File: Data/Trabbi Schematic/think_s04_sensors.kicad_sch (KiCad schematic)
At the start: 4 parts, among them SW1 Gear Selector (D7), U1 Motor Position Sensor (E05), U2 DC/DC High Effect Ref

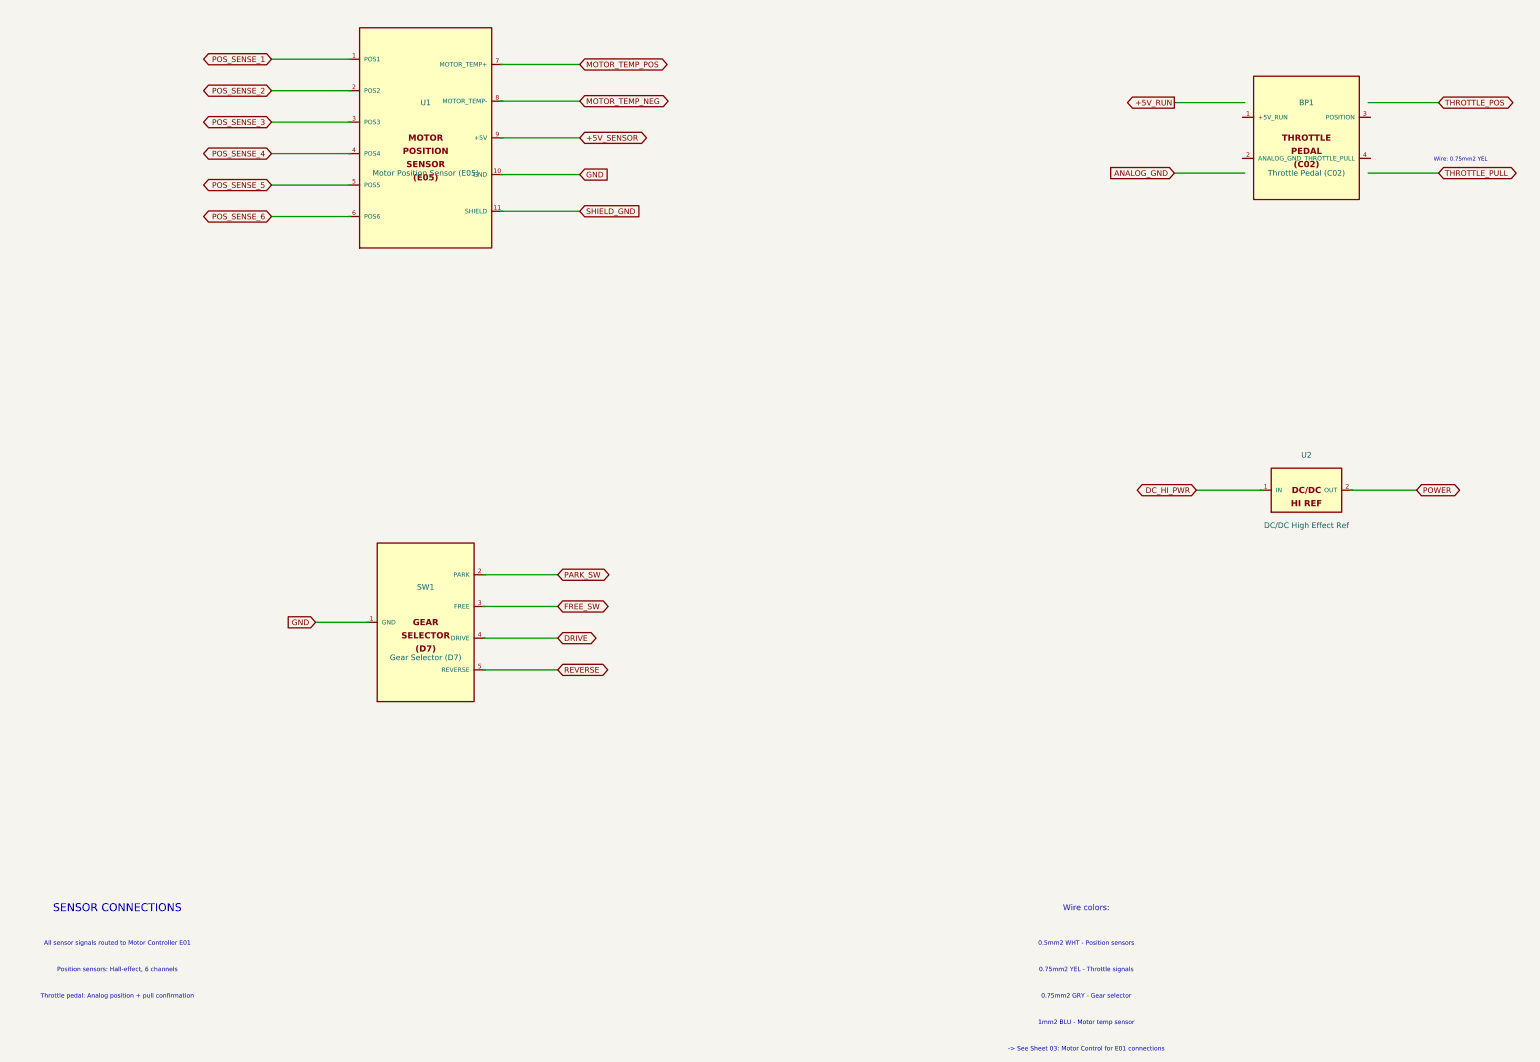
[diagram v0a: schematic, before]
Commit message: Fix wire-to-pin connections: use exact calculated pin positions
Refactored gen_think_complete.py to compute exact pin schematic
coordinates instead of using approximate manual offsets. Added p()
method to Sheet class that transforms symbol-local pin positions to
schematic coordinates. All 232 wire calls across 13 sub-sheet
generators now use p() for pin endpoints, fixing misaligned
connections (previously off by 0.54-10+ units).

Co-Authored-By: Claude Opus 4.6 <noreply@anthropic.com>
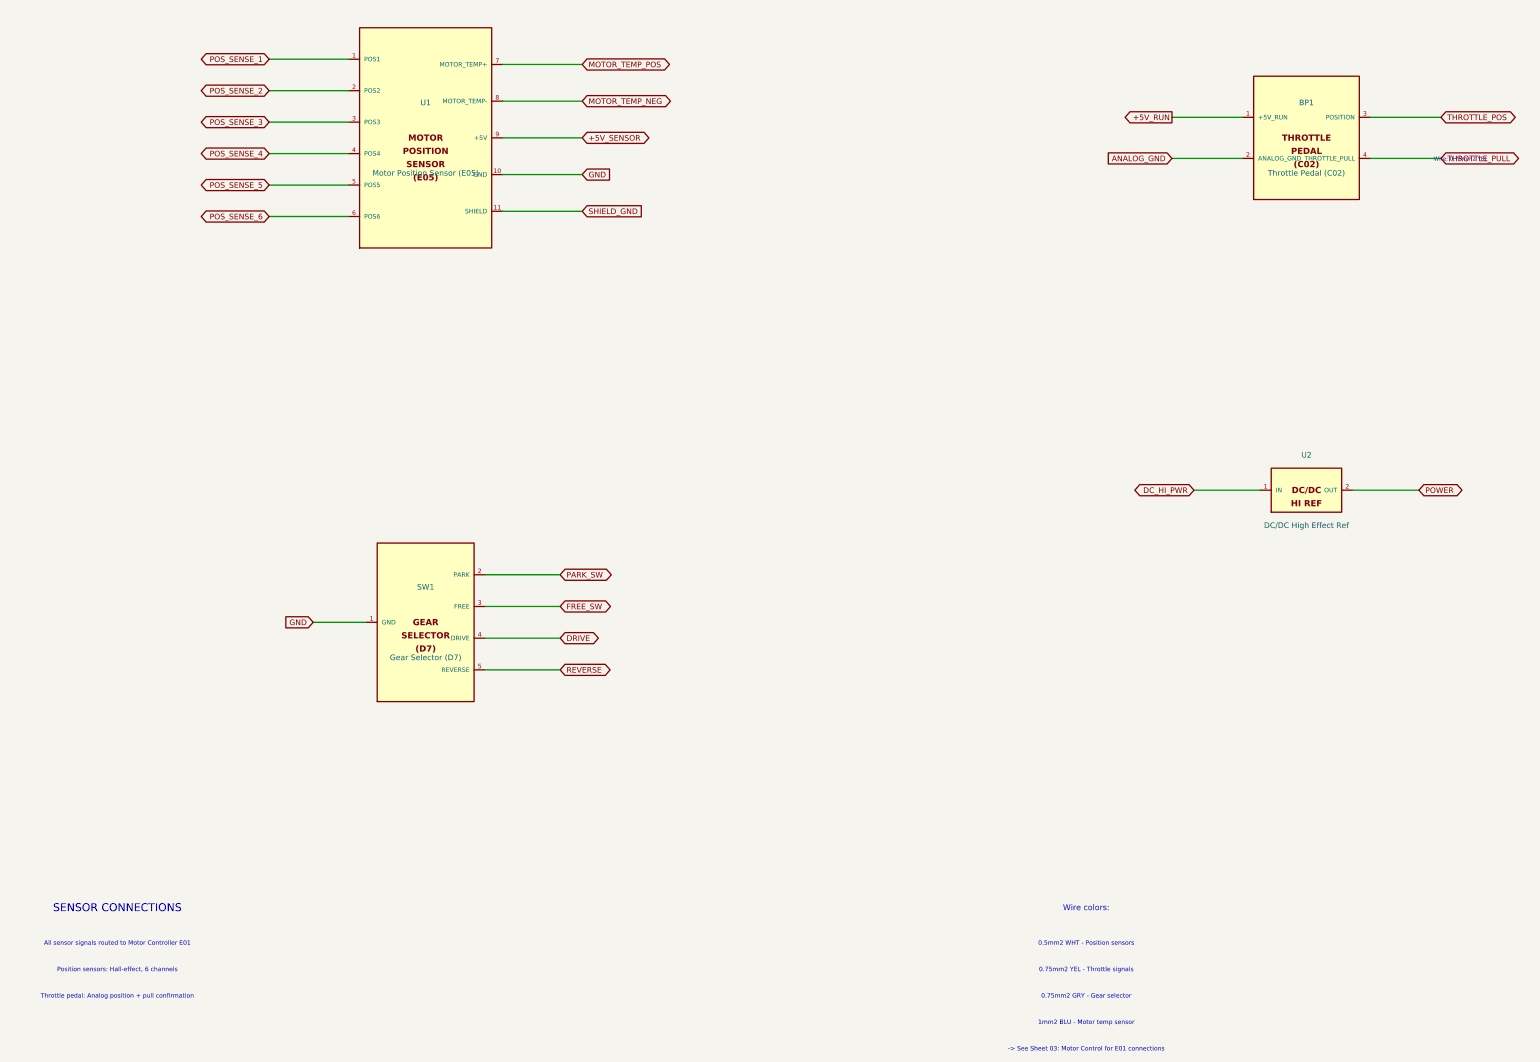
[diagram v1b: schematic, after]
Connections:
- net +5V_RUN: now also BP1.1 (+5V_RUN)
- net +5V_SENSOR: now also U1.9 (+5V)
- net ANALOG_GND: now also BP1.2 (ANALOG_GND)
- net DC_HI_PWR: now also U2.1 (IN)
- net DRIVE: now also SW1.4 (DRIVE)
- net FREE_SW: now also SW1.3 (FREE)
- net GND: now also SW1.1 (GND), U1.10 (GND)
- net MOTOR_TEMP_NEG: now also U1.8 (MOTOR_TEMP-)
- net MOTOR_TEMP_POS: now also U1.7 (MOTOR_TEMP+)
- net PARK_SW: now also SW1.2 (PARK)
- net POS_SENSE_1: now also U1.1 (POS1)
- net POS_SENSE_2: now also U1.2 (POS2)
- net POS_SENSE_3: now also U1.3 (POS3)
- net POS_SENSE_4: now also U1.4 (POS4)
- net POS_SENSE_5: now also U1.5 (POS5)
- net POS_SENSE_6: now also U1.6 (POS6)
- net POWER: now also U2.2 (OUT)
- net REVERSE: now also SW1.5 (REVERSE)
- net SHIELD_GND: now also U1.11 (SHIELD)
- net THROTTLE_POS: now also BP1.3 (POSITION)
- net THROTTLE_PULL: now also BP1.4 (THROTTLE_PULL)

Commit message: Enforce orthogonal routing and 1.27mm grid alignment
- Add _g() grid snap function to Sheet class (rounds all coordinates to nearest 1.27mm)
- Add wire_l() method for L-shaped orthogonal routing (horizontal+vertical segments)
- Apply grid snapping in p(), place(), wire(), label(), glabel(), junction(), no_connect(), defsym()
- Replace all 19 diagonal wire calls with wire_l() across S02, S06, S07, S08, S10, S12, S13
- All wire segments now strictly horizontal or vertical, no diagonals
- All coordinates verified on 1.27mm (50mil) KiCad standard grid

Co-Authored-By: Claude Opus 4.6 <noreply@anthropic.com>
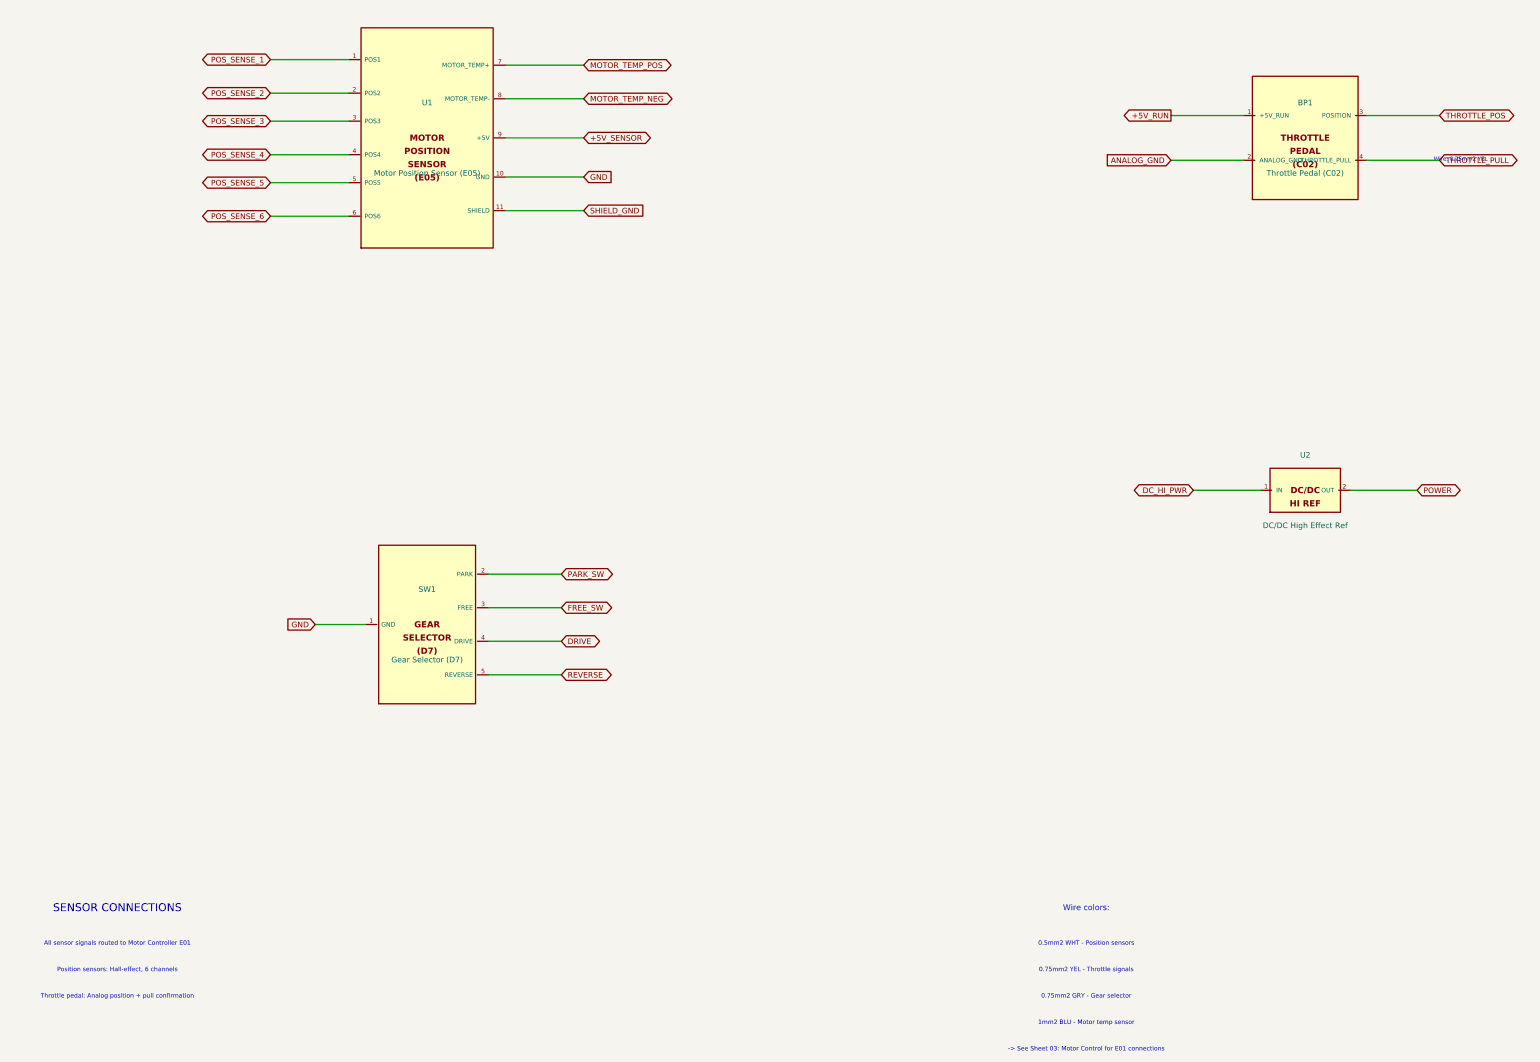
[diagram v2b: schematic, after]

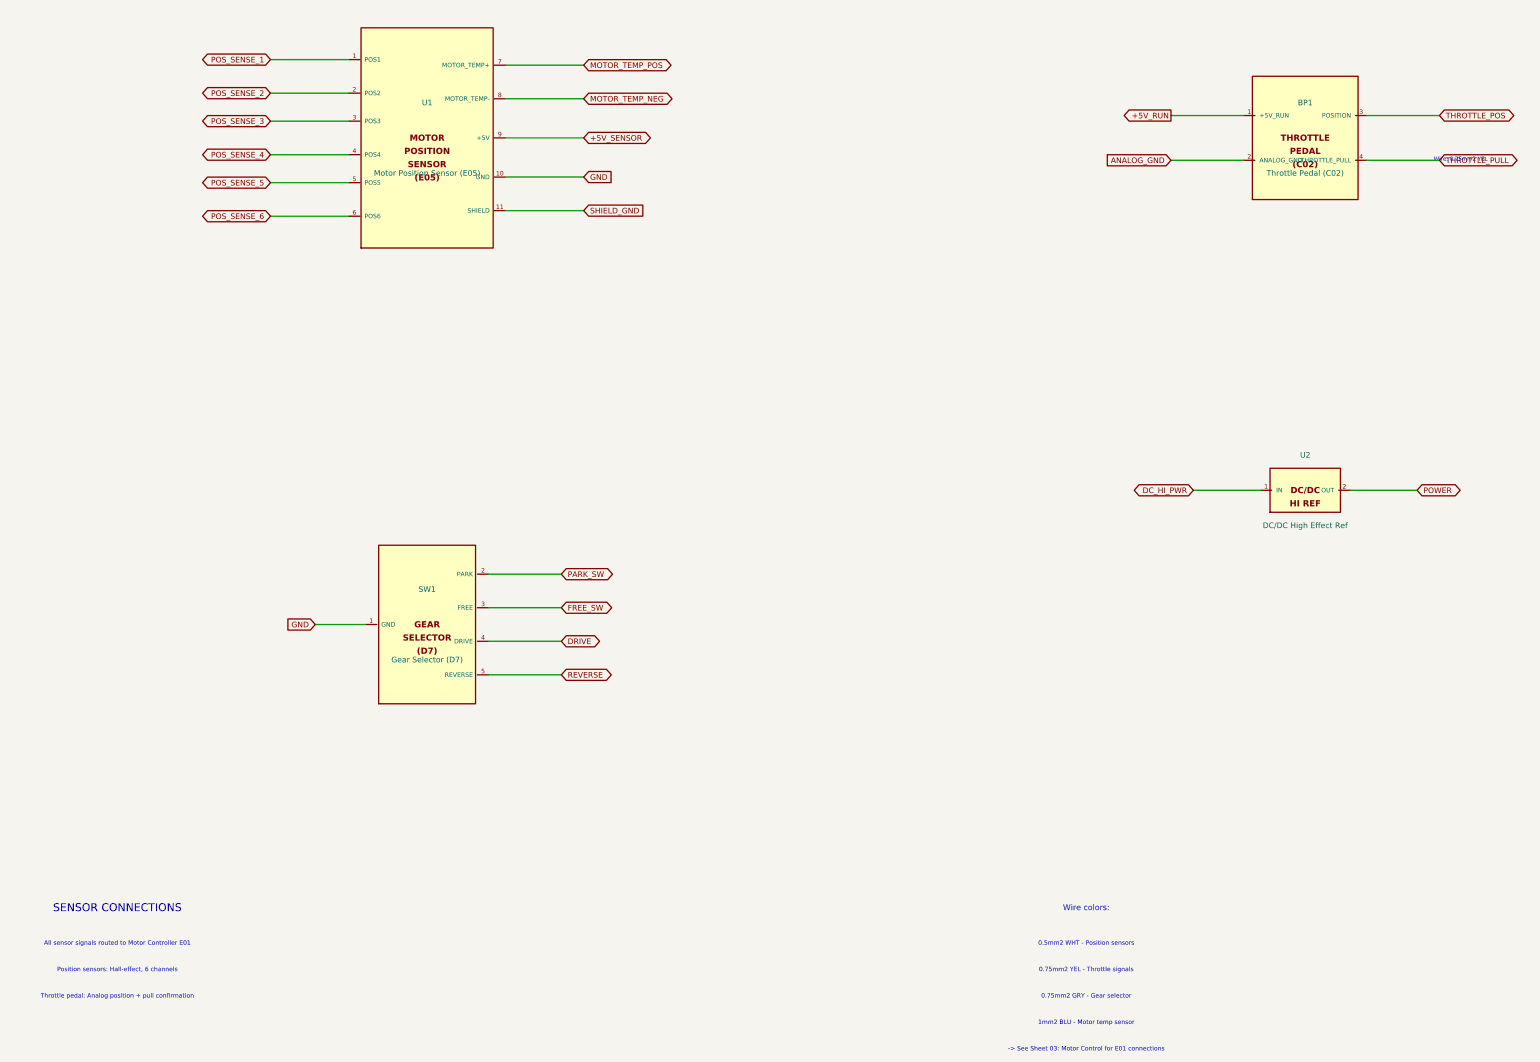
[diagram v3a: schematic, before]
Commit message: Fix label/text positioning: Ref/Value outside body, hide pin numbers
- Reference placed above body edge, Value below (dynamic based on
  symbol height) — no longer overlapping body text
- Pin numbers hidden (clutter, not useful in schematic view)
- Pin name font reduced from 1.016mm to 0.762mm (less overlap)
- Pin length increased from 2.54mm to 3.81mm (more room for pin names
  between body edge and endpoint)
- Store symbol dimensions in _sym_dims for dynamic property placement

Co-Authored-By: Claude Opus 4.6 <noreply@anthropic.com>
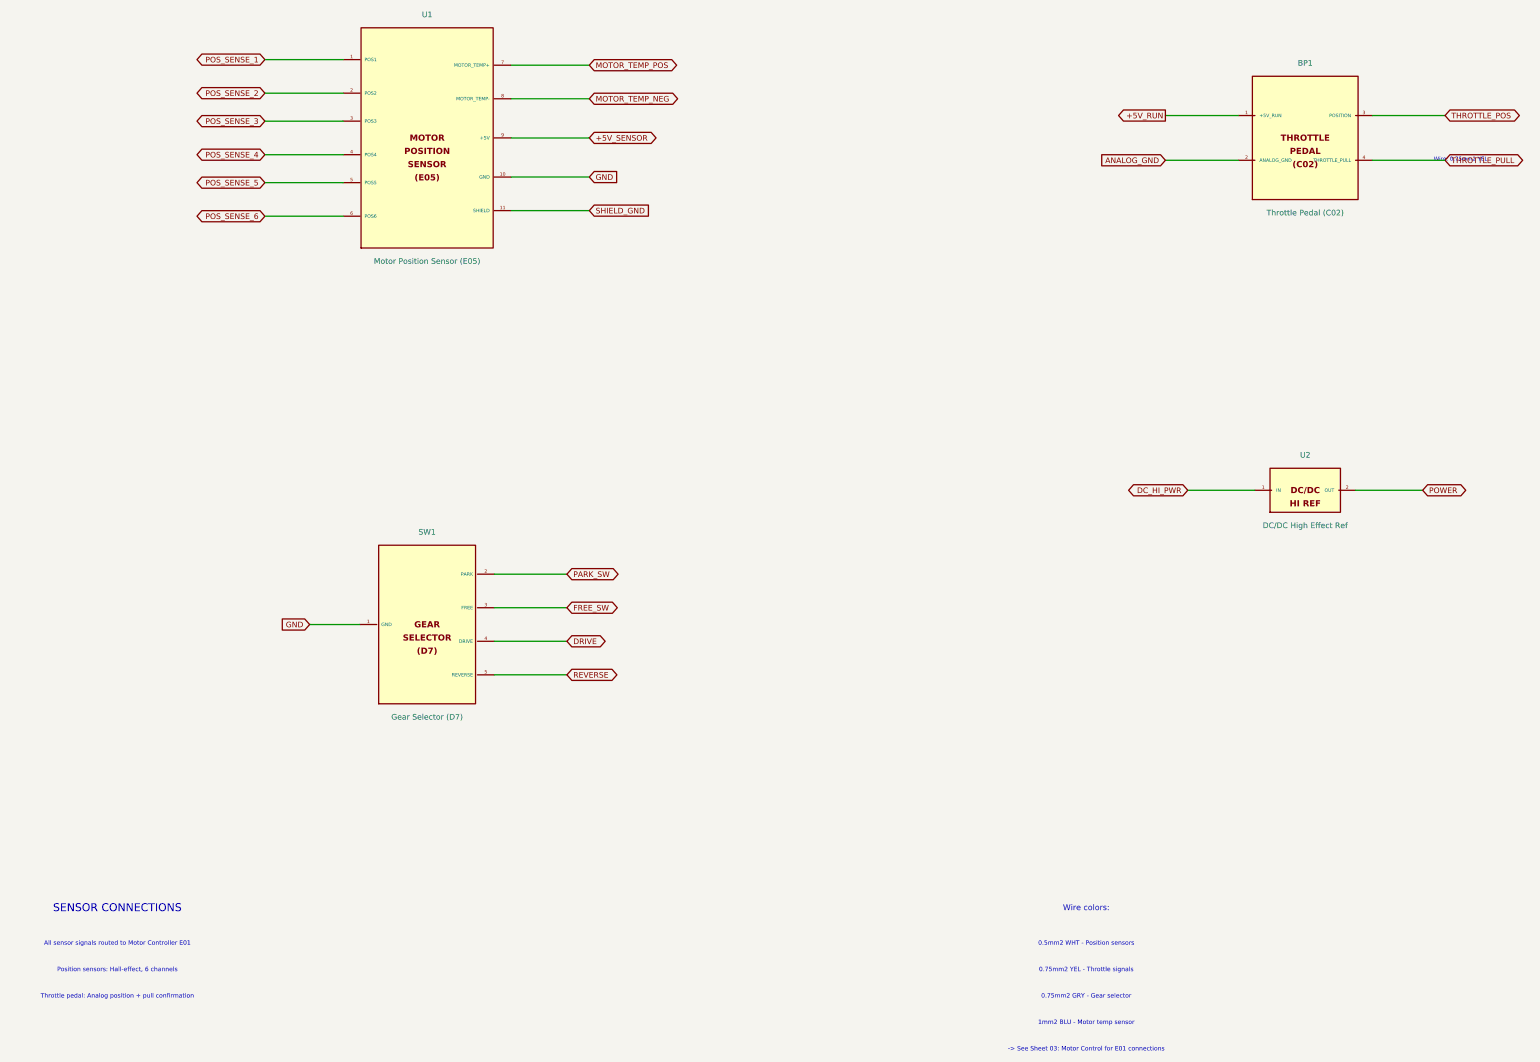
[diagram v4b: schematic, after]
